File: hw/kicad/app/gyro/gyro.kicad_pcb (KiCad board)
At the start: 2 copper layers, 8.8 x 12 mm, 14 parts, among them U1 ICM-42688-P, U2 BMI088

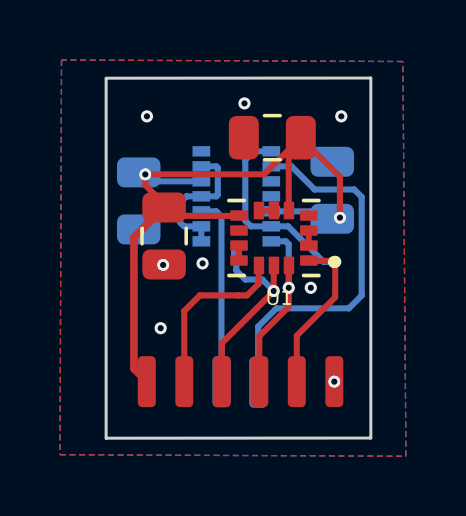
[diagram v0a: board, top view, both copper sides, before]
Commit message: 更新dc motor板
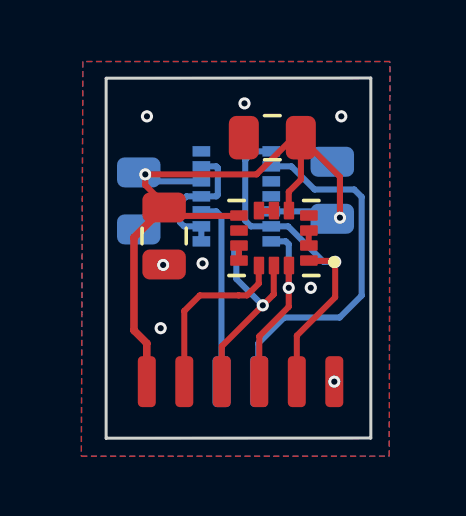
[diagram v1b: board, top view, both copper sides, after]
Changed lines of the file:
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@@
     (property "Sheetname" "")
     (attr smd)
-    (fp_text reference "U1" (at -0.176 -2.0048) (layer "F.SilkS")
+    (fp_text reference "U1" (at -0.176 -2.0048) (layer "F.SilkS") hide
         (effects (font (size 0.48 0.48) (thickness 0.15)))
     )
@@
   )
   (footprint "" (layer "B.Cu")
-    (at 53.7972 60.3504 180)
+    (at 53.8226 60.325 180)
     (fp_text reference "" (at 0 0) (layer "B.SilkS")
         (effects (font (size 1.27 1.27) (thickness 0.15)) (justify mirror))
@@
   (gr_line locked (start 57.5512 50.2088) (end 48.728 50.2144)
     (stroke (width 0.1) (type default)) (layer "Edge.Cuts"))
-  (segment (start 53.9948 53.4204) (end 55.2178 52.1974) (width 0.2032) (layer "F.Cu") (net 1))
+  (segment (start 50.0328 53.4204) (end 53.7422 53.4204) (width 0.2032) (layer "F.Cu") (net 1))
   (segment (start 50.661 54.4042) (end 50.661 54.524) (width 0.2032) (layer "F.Cu") (net 1))
-  (segment (start 54.8152 52.6) (end 55.2178 52.1974) (width 0.2032) (layer "F.Cu") (net 1))
+  (segment (start 49.6566 55.5284) (end 50.661 54.524) (width 0.254) (layer "F.Cu") (net 1))
   (segment (start 50.0328 53.4204) (end 50.0328 53.776) (width 0.2032) (layer "F.Cu") (net 1))
   (segment (start 55.2178 52.1974) (end 56.5214 53.501) (width 0.2032) (layer "F.Cu") (net 1))
   (segment (start 53.1502 54.8042) (end 50.9412 54.8042) (width 0.2032) (layer "F.Cu") (net 1))
-  (segment (start 50.0836 60.3292) (end 49.6566 59.9022) (width 0.254) (layer "F.Cu") (net 1))
-  (segment (start 49.6566 59.9022) (end 49.6566 55.5284) (width 0.254) (layer "F.Cu") (net 1))
+  (segment (start 49.6566 58.6232) (end 49.6566 55.5284) (width 0.254) (layer "F.Cu") (net 1))
+  (segment (start 54.9652 52.1974) (end 55.2178 52.1974) (width 0.2032) (layer "F.Cu") (net 1))
+  (segment (start 55.2196 53.594) (end 55.2196 52.1992) (width 0.2032) (layer "F.Cu") (net 1))
+  (segment (start 54.8152 53.9984) (end 55.2196 53.594) (width 0.2032) (layer "F.Cu") (net 1))
   (segment (start 50.9412 54.8042) (end 50.661 54.524) (width 0.2032) (layer "F.Cu") (net 1))
-  (segment (start 54.8152 54.6392) (end 54.8152 52.6) (width 0.2032) (layer "F.Cu") (net 1))
+  (segment (start 50.0836 59.0502) (end 49.6566 58.6232) (width 0.254) (layer "F.Cu") (net 1))
   (segment (start 56.5214 53.501) (end 56.5214 54.864) (width 0.2032) (layer "F.Cu") (net 1))
-  (segment (start 50.0328 53.4204) (end 53.9948 53.4204) (width 0.2032) (layer "F.Cu") (net 1))
+  (segment (start 53.7422 53.4204) (end 54.9652 52.1974) (width 0.2032) (layer "F.Cu") (net 1))
   (segment (start 50.0328 53.776) (end 50.661 54.4042) (width 0.2032) (layer "F.Cu") (net 1))
-  (segment (start 49.6566 55.5284) (end 50.661 54.524) (width 0.254) (layer "F.Cu") (net 1))
+  (segment (start 54.8152 54.6392) (end 54.8152 53.9984) (width 0.2032) (layer "F.Cu") (net 1))
+  (segment (start 55.2196 52.1992) (end 55.2178 52.1974) (width 0.2032) (layer "F.Cu") (net 1))
+  (segment (start 50.0836 60.3292) (end 50.0836 59.0502) (width 0.254) (layer "F.Cu") (net 1))
   (via (at 50.0328 53.4204) (size 0.4064) (drill 0.2032) (layers "F.Cu" "B.Cu") (net 1))
   (via (at 56.5214 54.864) (size 0.4064) (drill 0.2032) (layers "F.Cu" "B.Cu") (net 1))
@@
   (segment (start 53.142919 57.4548) (end 53.4226 57.4548) (width 0.2032) (layer "F.Cu") (net 3))
   (segment (start 53.142919 57.4548) (end 51.8522 57.4548) (width 0.2032) (layer "F.Cu") (net 3))
-  (segment (start 54.3152 57.3076) (end 54.3152 57.3178) (width 0.2032) (layer "F.Cu") (net 4))
-  (segment (start 54.3152 57.3178) (end 52.5836 59.0494) (width 0.2032) (layer "F.Cu") (net 4))
-  (segment (start 54.3152 56.4692) (end 54.3152 57.3076) (width 0.2032) (layer "F.Cu") (net 4))
-  (segment (start 52.5836 59.0494) (end 52.5836 60.3292) (width 0.2032) (layer "F.Cu") (net 4))
-  (via (at 54.3152 57.3076) (size 0.4064) (drill 0.2032) (layers "F.Cu" "B.Cu") (net 4))
-  (segment (start 53.3666 56.9256) (end 53.067 56.626) (width 0.2032) (layer "B.Cu") (net 4))
-  (segment (start 54.3152 57.3076) (end 53.9332 56.9256) (width 0.2032) (layer "B.Cu") (net 4))
-  (segment (start 53.067 56.626) (end 53.067 56.0678) (width 0.2032) (layer "B.Cu") (net 4))
-  (segment (start 53.9332 56.9256) (end 53.3666 56.9256) (width 0.2032) (layer "B.Cu") (net 4))
+  (segment (start 52.5836 59.151) (end 53.9496 57.785) (width 0.2032) (layer "F.Cu") (net 4))
+  (segment (start 54.3152 57.4194) (end 53.9496 57.785) (width 0.2032) (layer "F.Cu") (net 4))
+  (segment (start 52.5836 60.3292) (end 52.5836 59.151) (width 0.2032) (layer "F.Cu") (net 4))
+  (segment (start 54.3152 56.4692) (end 54.3152 57.4194) (width 0.2032) (layer "F.Cu") (net 4))
+  (via (at 53.9496 57.785) (size 0.4064) (drill 0.2032) (layers "F.Cu" "B.Cu") (net 4))
+  (segment (start 53.067 56.9024) (end 53.9496 57.785) (width 0.2032) (layer "B.Cu") (net 4))
+  (segment (start 53.067 56.0678) (end 53.067 56.9024) (width 0.2032) (layer "B.Cu") (net 4))
   (segment (start 54.8152 57.8338) (end 54.8152 56.4692) (width 0.2032) (layer "F.Cu") (net 5))
   (segment (start 53.8336 58.8154) (end 54.8152 57.8338) (width 0.2032) (layer "F.Cu") (net 5))
@@
   (segment (start 51.902 54.6528) (end 52.4002 54.6528) (width 0.2032) (layer "B.Cu") (net 12))
   (segment (start 55.6768 53.9242) (end 56.9976 53.9242) (width 0.2032) (layer "B.Cu") (net 14))
+  (segment (start 56.9976 53.9242) (end 57.2464 54.173) (width 0.2032) (layer "B.Cu") (net 14))
+  (segment (start 57.2464 54.173) (end 57.2464 57.46) (width 0.2032) (layer "B.Cu") (net 14))
+  (segment (start 53.7972 59.055) (end 53.7972 60.3504) (width 0.2032) (layer "B.Cu") (net 14))
+  (segment (start 56.515 58.1914) (end 54.6608 58.1914) (width 0.2032) (layer "B.Cu") (net 14))
+  (segment (start 57.2464 57.46) (end 56.515 58.1914) (width 0.2032) (layer "B.Cu") (net 14))
+  (segment (start 54.9054 53.1528) (end 55.6768 53.9242) (width 0.2032) (layer "B.Cu") (net 14))
+  (segment (start 54.6608 58.1914) (end 53.7972 59.055) (width 0.2032) (layer "B.Cu") (net 14))
   (segment (start 54.232 53.1528) (end 54.9054 53.1528) (width 0.2032) (layer "B.Cu") (net 14))
-  (segment (start 56.8198 57.8866) (end 54.4068 57.8866) (width 0.2032) (layer "B.Cu") (net 14))
-  (segment (start 56.9976 53.9242) (end 57.2464 54.173) (width 0.2032) (layer "B.Cu") (net 14))
-  (segment (start 53.7972 58.4962) (end 53.7972 60.3504) (width 0.2032) (layer "B.Cu") (net 14))
-  (segment (start 54.9054 53.1528) (end 55.6768 53.9242) (width 0.2032) (layer "B.Cu") (net 14))
-  (segment (start 57.2464 54.173) (end 57.2464 57.46) (width 0.2032) (layer "B.Cu") (net 14))
-  (segment (start 54.4068 57.8866) (end 53.7972 58.4962) (width 0.2032) (layer "B.Cu") (net 14))
-  (segment (start 57.2464 57.46) (end 56.8198 57.8866) (width 0.2032) (layer "B.Cu") (net 14))
-  (zone (net 2) (net_name "GND") (layers "F&B.Cu") (hatch none 0.254)
-    (connect_pads yes (clearance 0.1524))
-    (min_thickness 0.1524) (filled_areas_thickness no)
-    (fill yes (thermal_gap 0.254) (thermal_bridge_width 0.254) (smoothing fillet) (radius 0.127))
+  (zone (net 2) (net_name "GND") (layers "F&B.Cu") (hatch none 0.127)
+    (connect_pads yes (clearance 0.127))
+    (min_thickness 0.127) (filled_areas_thickness no)
+    (fill yes (thermal_gap 0.127) (thermal_bridge_width 0.254) (smoothing fillet) (radius 0.127))
     (polygon
       (pts
-        (xy 47.241066 49.607669)
-        (xy 47.190266 62.764869)
-        (xy 58.721866 62.815669)
-        (xy 58.620266 49.658469)
+        (xy 47.952266 49.658469)
+        (xy 47.901466 62.815669)
+        (xy 58.166 62.8142)
+        (xy 58.188466 49.658469)
       )
     )

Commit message: 更新gyro
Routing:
- net GND: vias 8 -> 6
